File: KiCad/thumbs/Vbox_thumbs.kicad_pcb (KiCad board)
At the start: 2 copper layers, 67 x 46.5 mm, 12 parts, among them J1 Conn_01x06, J2 Conn_01x06, SW1 SW_Push_45deg, SW10 SW_Push_45deg, SW2 SW_Push_45deg, SW3 SW_Push_45deg, SW4 SW_Push_45deg, SW5 SW_Push_45deg, SW6 SW_Push_45deg, SW7 SW_Push_45deg, SW8 SW_Push_45deg, SW9 SW_Push_45deg

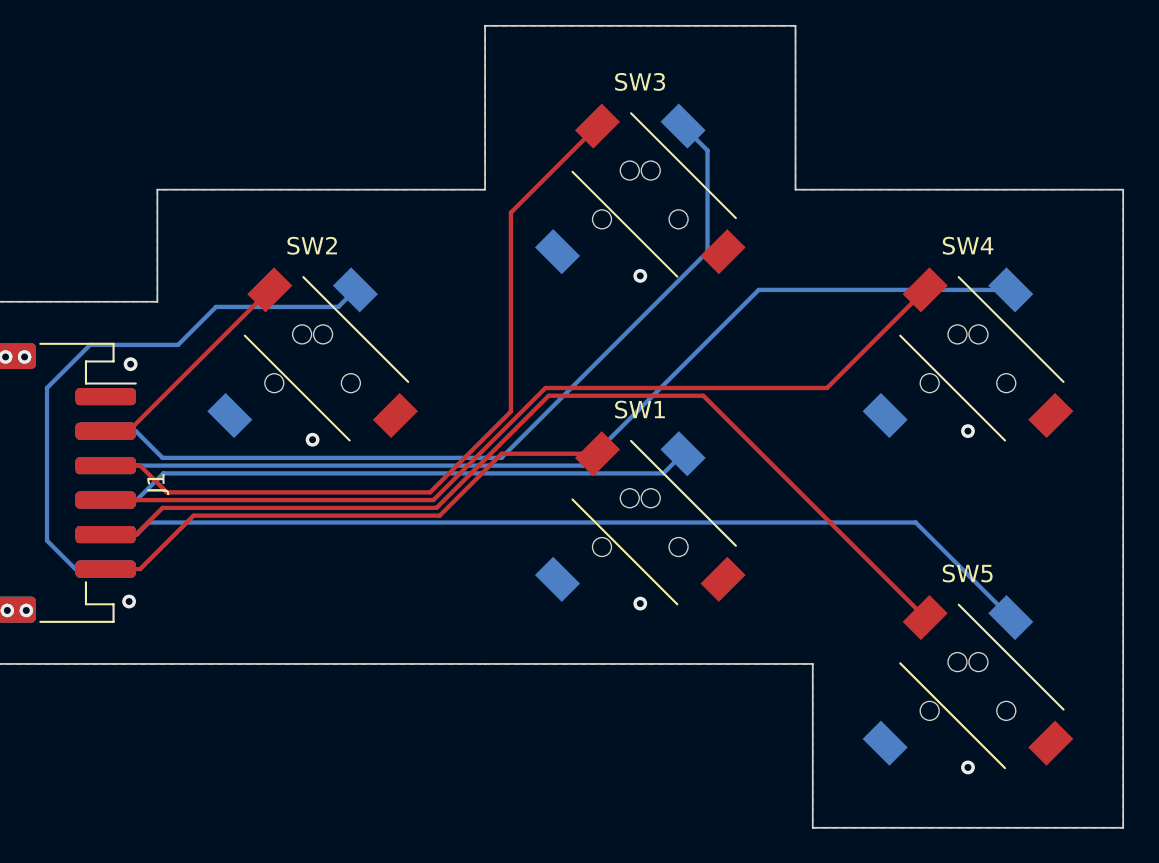
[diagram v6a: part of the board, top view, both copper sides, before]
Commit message: make both sides share holes
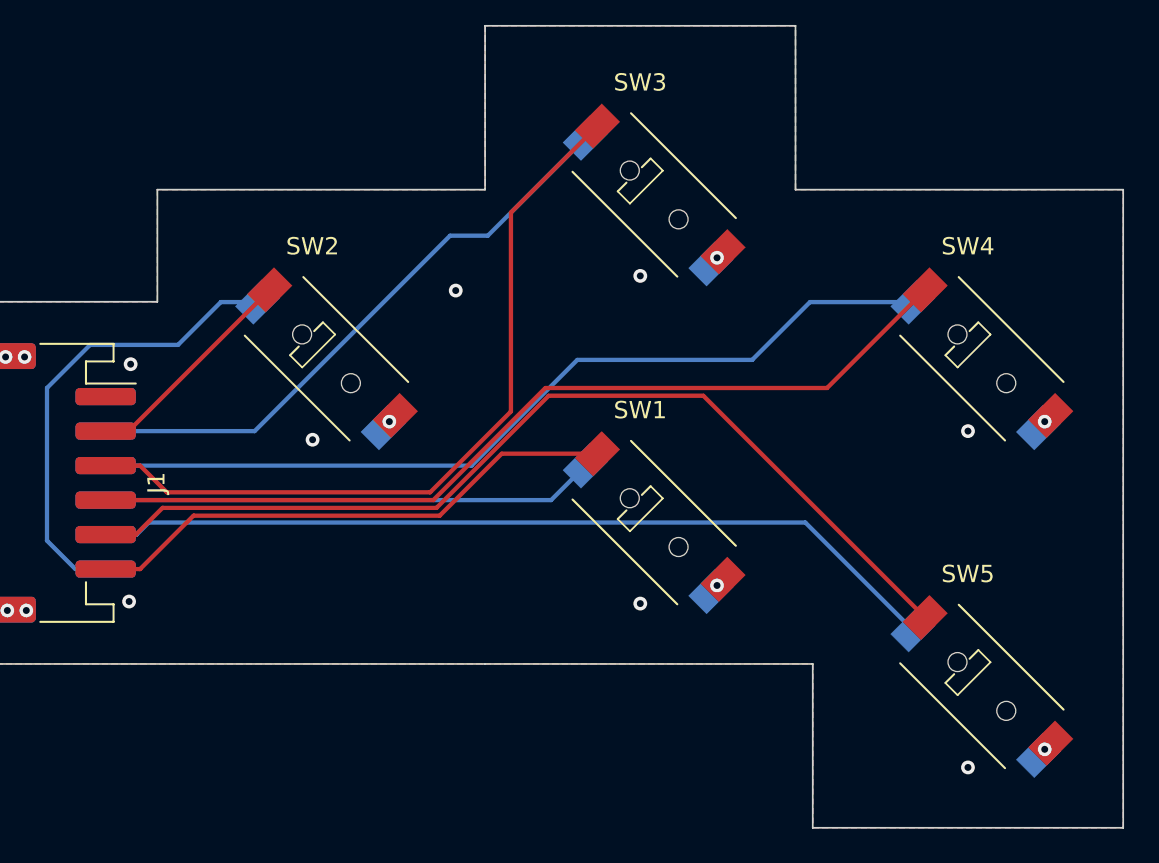
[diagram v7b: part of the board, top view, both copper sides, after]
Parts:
- SW10, SW6, SW7, SW8, SW9: footprint Buttons:Vbox -> Buttons:Vbox_1
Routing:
- net C_UP: track 48.4 -> 34.8 mm
- net C_LT: track 56.7 -> 50.7 mm
- net A: track 34.6 -> 28.6 mm
- net C_RT: track 33.2 -> 27.2 mm
- net C_DN: track 55.1 -> 49.7 mm
- net GND: vias 13 -> 19

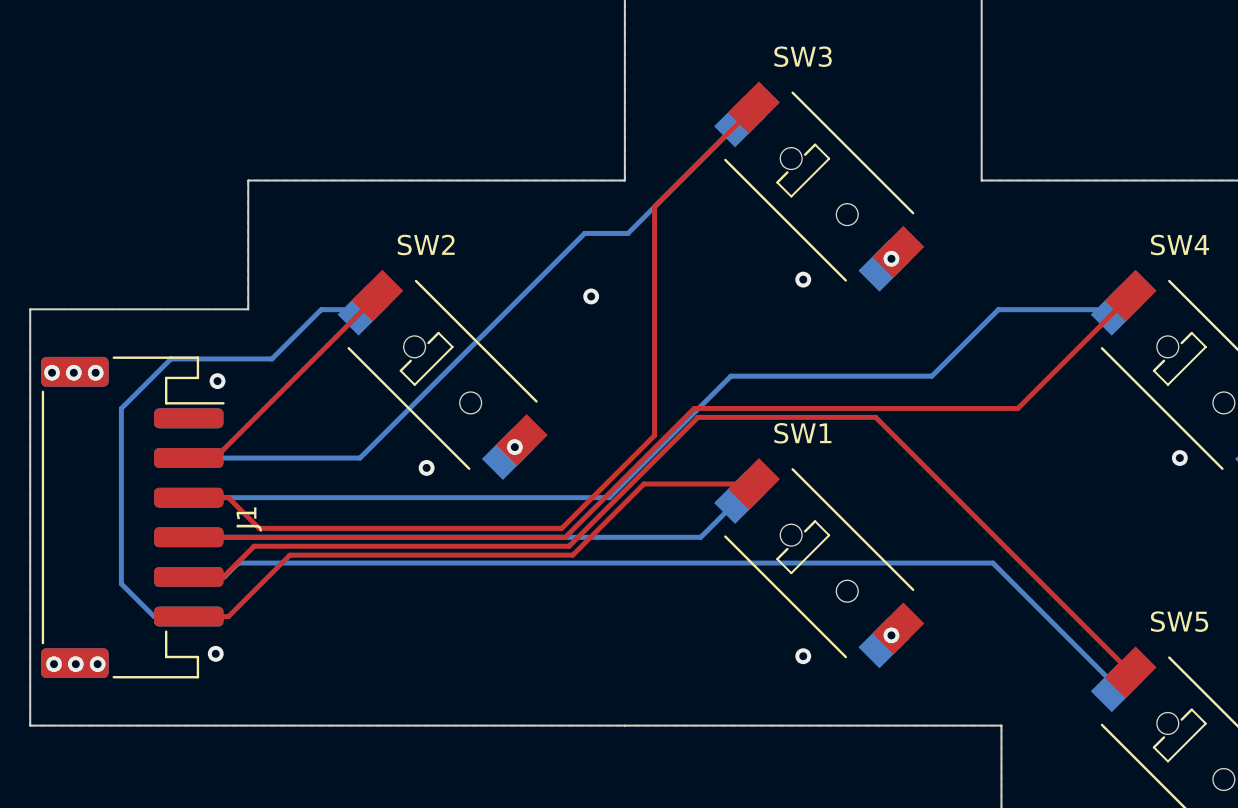
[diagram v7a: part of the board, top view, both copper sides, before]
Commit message: flip connectors
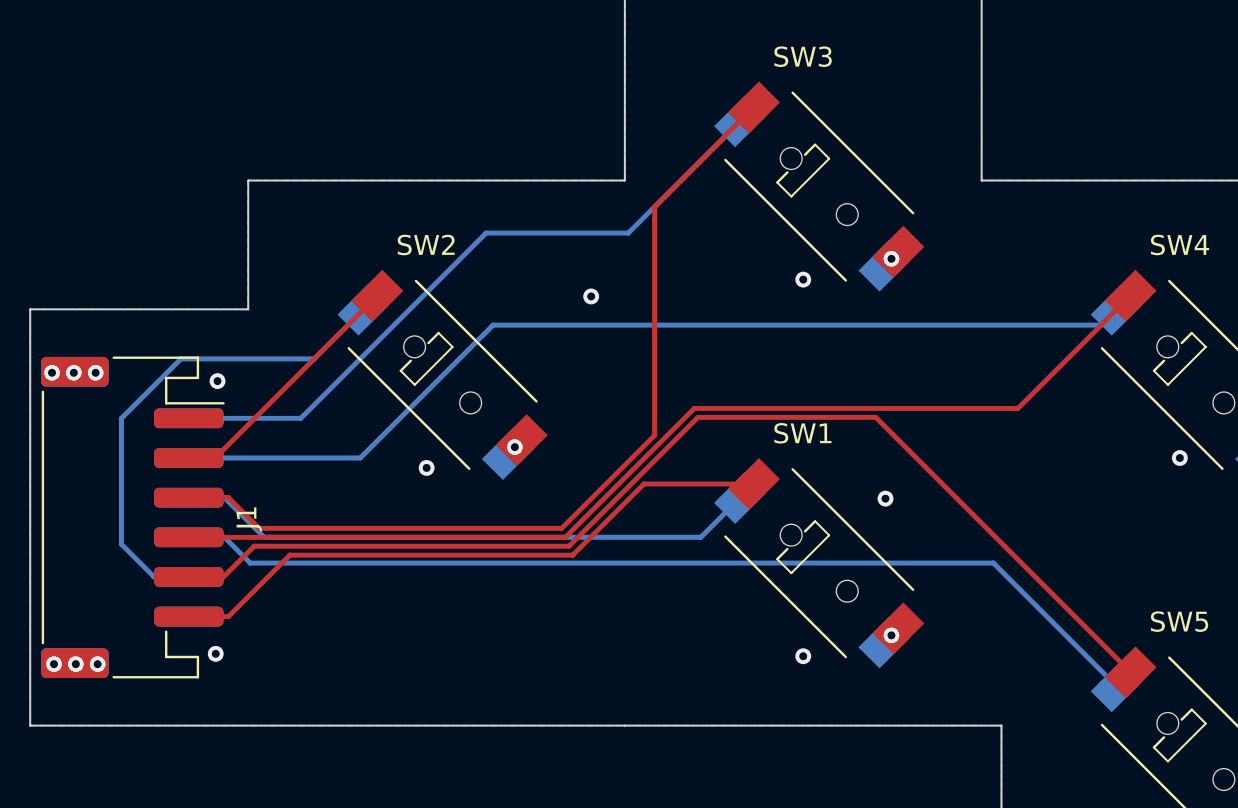
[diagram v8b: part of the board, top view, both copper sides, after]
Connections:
- J2 pad 1: C_RT -> GND
- J2 pad 2: C_DN -> C_RT
- J2 pad 3: A -> C_DN
- J2 pad 4: C_LT -> A
- J2 pad 5: C_UP -> C_LT
- J2 pad 6: GND -> C_UP
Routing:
- net C_RT: track 27.2 -> 24.9 mm
- net C_UP: track 34.8 -> 34.0 mm
- net A: track 28.6 -> 29.5 mm
- net C_LT: track 50.7 -> 49.9 mm
- net GND: vias 19 -> 20
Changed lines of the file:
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@@
       (stroke (width 0.1) (type solid)) (layer "B.Fab"))
     (pad "1" smd roundrect (at -5 2.85 90) (size 1 3.5) (layers "B.Cu" "B.Paste" "B.Mask") (roundrect_rratio 0.25)
-      (net 11 "C_RT") (pinfunction "Pin_1") (pintype "passive"))
+      (net 1 "GND") (pinfunction "Pin_1") (pintype "passive") (thermal_bridge_width 0.2) (thermal_gap 0.7))
     (pad "2" smd roundrect (at -3 2.85 90) (size 1 3.5) (layers "B.Cu" "B.Paste" "B.Mask") (roundrect_rratio 0.25)
-      (net 10 "C_DN") (pinfunction "Pin_2") (pintype "passive"))
+      (net 11 "C_RT") (pinfunction "Pin_2") (pintype "passive"))
     (pad "3" smd roundrect (at -1 2.85 90) (size 1 3.5) (layers "B.Cu" "B.Paste" "B.Mask") (roundrect_rratio 0.25)
-      (net 9 "A") (pinfunction "Pin_3") (pintype "passive"))
+      (net 10 "C_DN") (pinfunction "Pin_3") (pintype "passive"))
     (pad "4" smd roundrect (at 1 2.85 90) (size 1 3.5) (layers "B.Cu" "B.Paste" "B.Mask") (roundrect_rratio 0.25)
-      (net 8 "C_LT") (pinfunction "Pin_4") (pintype "passive"))
+      (net 9 "A") (pinfunction "Pin_4") (pintype "passive"))
     (pad "5" smd roundrect (at 3 2.85 90) (size 1 3.5) (layers "B.Cu" "B.Paste" "B.Mask") (roundrect_rratio 0.25)
-      (net 7 "C_UP") (pinfunction "Pin_5") (pintype "passive"))
+      (net 8 "C_LT") (pinfunction "Pin_5") (pintype "passive"))
     (pad "6" smd roundrect (at 5 2.85 90) (size 1 3.5) (layers "B.Cu" "B.Paste" "B.Mask") (roundrect_rratio 0.25)
-      (net 1 "GND") (pinfunction "Pin_6") (pintype "passive") (thermal_bridge_width 0.2) (thermal_gap 0.7))
+      (net 7 "C_UP") (pinfunction "Pin_6") (pintype "passive") (thermal_bridge_width 0.2) (thermal_gap 0.7))
     (pad "MP" smd roundrect (at -7.35 -2.9 90) (size 1.5 3.4) (layers "B.Cu" "B.Paste" "B.Mask") (roundrect_rratio 0.166667)
       (net 1 "GND") (thermal_gap 1))
@@
   (via (at 89.36 114.88) (size 0.8) (drill 0.4) (layers "F.Cu" "B.Cu") (free) (net 1))
   (via (at 123.45 113.95) (size 0.8) (drill 0.4) (layers "F.Cu" "B.Cu") (free) (net 1))
+  (via (at 123.15 107.05) (size 0.8) (drill 0.4) (layers "F.Cu" "B.Cu") (free) (net 1))
   (via (at 83.3 100.7) (size 0.8) (drill 0.4) (layers "F.Cu" "B.Cu") (net 1))
   (via (at 82.3 115.4) (size 0.8) (drill 0.4) (layers "F.Cu" "B.Cu") (net 1))
@@
   (segment (start 107.186396 109.45) (end 113.686396 102.95) (width 0.25) (layer "F.Cu") (net 6))
   (segment (start 113.686396 102.95) (end 122.657107 102.95) (width 0.25) (layer "F.Cu") (net 6))
-  (segment (start 107.97 93.67) (end 110.159005 93.67) (width 0.25) (layer "B.Cu") (net 7))
-  (segment (start 110.159005 93.67) (end 115.810949 88.018056) (width 0.25) (layer "B.Cu") (net 7))
-  (segment (start 96.64 105) (end 107.97 93.67) (width 0.25) (layer "B.Cu") (net 7))
-  (segment (start 88 105) (end 96.64 105) (width 0.25) (layer "B.Cu") (net 7))
-  (segment (start 88 107) (end 109.22 107) (width 0.25) (layer "B.Cu") (net 8))
-  (segment (start 125.49 100.87) (end 128.841944 97.518056) (width 0.25) (layer "B.Cu") (net 8))
-  (segment (start 128.841944 97.518056) (end 134.810949 97.518056) (width 0.25) (layer "B.Cu") (net 8))
-  (segment (start 115.35 100.87) (end 125.49 100.87) (width 0.25) (layer "B.Cu") (net 8))
-  (segment (start 109.22 107) (end 115.35 100.87) (width 0.25) (layer "B.Cu") (net 8))
+  (segment (start 93.65 103) (end 103 93.65) (width 0.25) (layer "B.Cu") (net 7))
+  (segment (start 103 93.65) (end 110.179005 93.65) (width 0.25) (layer "B.Cu") (net 7))
+  (segment (start 88 103) (end 93.65 103) (width 0.25) (layer "B.Cu") (net 7))
+  (segment (start 110.179005 93.65) (end 115.810949 88.018056) (width 0.25) (layer "B.Cu") (net 7))
+  (segment (start 103.354126 98.295874) (end 134.033131 98.295874) (width 0.25) (layer "B.Cu") (net 8))
+  (segment (start 96.65 105) (end 103.354126 98.295874) (width 0.25) (layer "B.Cu") (net 8))
+  (segment (start 88 105) (end 96.65 105) (width 0.25) (layer "B.Cu") (net 8))
+  (segment (start 134.033131 98.295874) (end 134.810949 97.518056) (width 0.25) (layer "B.Cu") (net 8))
+  (segment (start 91.8 109) (end 113.829005 109) (width 0.25) (layer "B.Cu") (net 9))
   (segment (start 113.829005 109) (end 115.810949 107.018056) (width 0.25) (layer "B.Cu") (net 9))
-  (segment (start 88 109) (end 113.829005 109) (width 0.25) (layer "B.Cu") (net 9))
-  (segment (start 89.8 111) (end 90.5 110.3) (width 0.25) (layer "B.Cu") (net 10))
-  (segment (start 128.57 110.3) (end 134.788056 116.518056) (width 0.25) (layer "B.Cu") (net 10))
-  (segment (start 88 111) (end 89.8 111) (width 0.25) (layer "B.Cu") (net 10))
-  (segment (start 134.788056 116.518056) (end 134.810949 116.518056) (width 0.25) (layer "B.Cu") (net 10))
-  (segment (start 90.5 110.3) (end 128.57 110.3) (width 0.25) (layer "B.Cu") (net 10))
-  (segment (start 92.2 100) (end 94.681944 97.518056) (width 0.25) (layer "B.Cu") (net 11))
-  (segment (start 87.1 100) (end 92.2 100) (width 0.25) (layer "B.Cu") (net 11))
-  (segment (start 84.6 102.5) (end 87.1 100) (width 0.25) (layer "B.Cu") (net 11))
-  (segment (start 88 113) (end 86.25 113) (width 0.25) (layer "B.Cu") (net 11))
-  (segment (start 94.681944 97.518056) (end 96.810949 97.518056) (width 0.25) (layer "B.Cu") (net 11))
-  (segment (start 84.6 111.35) (end 84.6 102.5) (width 0.25) (layer "B.Cu") (net 11))
-  (segment (start 86.25 113) (end 84.6 111.35) (width 0.25) (layer "B.Cu") (net 11))
+  (segment (start 88 107) (end 89.8 107) (width 0.25) (layer "B.Cu") (net 9))
+  (segment (start 89.8 107) (end 91.8 109) (width 0.25) (layer "B.Cu") (net 9))
+  (segment (start 89.8 109) (end 91.1 110.3) (width 0.25) (layer "B.Cu") (net 10))
+  (segment (start 88 109) (end 89.8 109) (width 0.25) (layer "B.Cu") (net 10))
+  (segment (start 91.1 110.3) (end 128.592893 110.3) (width 0.25) (layer "B.Cu") (net 10))
+  (segment (start 128.592893 110.3) (end 134.810949 116.518056) (width 0.25) (layer "B.Cu") (net 10))
+  (segment (start 86.25 111) (end 84.6 109.35) (width 0.25) (layer "B.Cu") (net 11))
+  (segment (start 88 111) (end 86.25 111) (width 0.25) (layer "B.Cu") (net 11))
+  (segment (start 84.6 109.35) (end 84.6 103) (width 0.25) (layer "B.Cu") (net 11))
+  (segment (start 87.6 100) (end 94.329005 100) (width 0.25) (layer "B.Cu") (net 11))
+  (segment (start 84.6 103) (end 87.6 100) (width 0.25) (layer "B.Cu") (net 11))
+  (segment (start 94.329005 100) (end 96.810949 97.518056) (width 0.25) (layer "B.Cu") (net 11))
   (zone (net 1) (net_name "GND") (layer "F.Cu") (hatch edge 0.5)
     (connect_pads (clearance 0.15))
